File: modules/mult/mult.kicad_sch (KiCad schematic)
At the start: 9 parts, among them J1 Thonkiconn, J2 Thonkiconn, J3 Thonkiconn, J4 Thonkiconn, J5 Thonkiconn, J6 Thonkiconn, J7 Thonkiconn, J8 Thonkiconn

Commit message: Generate KiCad projects from Haskell: pcbgen toolkit, regenerated mult
toolkit/ is a cabal project that turns a design description
(toolkit/src/Designs/<Name>.hs) into a complete KiCad 10 project: schematic
with embedded library symbols, board with embedded library footprints, project
file with design rules, and custom DRC rules. UUIDs are derived from stable
seeds so regeneration is byte-identical. toolkit/check.sh runs ERC, DRC with
zone refill and schematic parity on a copy in build/, and renders both sides.

modules/mult is now generated. With --severity-all it has zero ERC violations,
zero DRC violations, zero unconnected items and zero parity issues. The
Konnect-made board it replaces had nine library-mismatch warnings and needed
GUI steps to finish.

README.md explains the tool choices (KiCad as compile target, kicad-cli,
KiKit for fab export, Konnect read-only). SETUP.md and CLAUDE.md follow the
new workflow.

Co-Authored-By: Claude Fable 5.1 <noreply@anthropic.com>
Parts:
- JP1: now left out of the parts list
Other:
- note added: "MULT - passive 2x4 multiple, 4HP J1-J4 = group A, J5-J8 = group B. Bridge JP1 (back of PCB) to join both groups into one 1x8 multiple. Jack switch (TN) pins intentionally unconnected."
- note removed: "MULT - passive 2x4 multiple, 4HP J1-J4 = group A, J5-J8 = group B. Bridge JP1 to join both groups into one 1x8 multiple. Jack switch (TN) pins intentionally unconnected."
- title: (none) -> MULT - passive 2x4 multiple

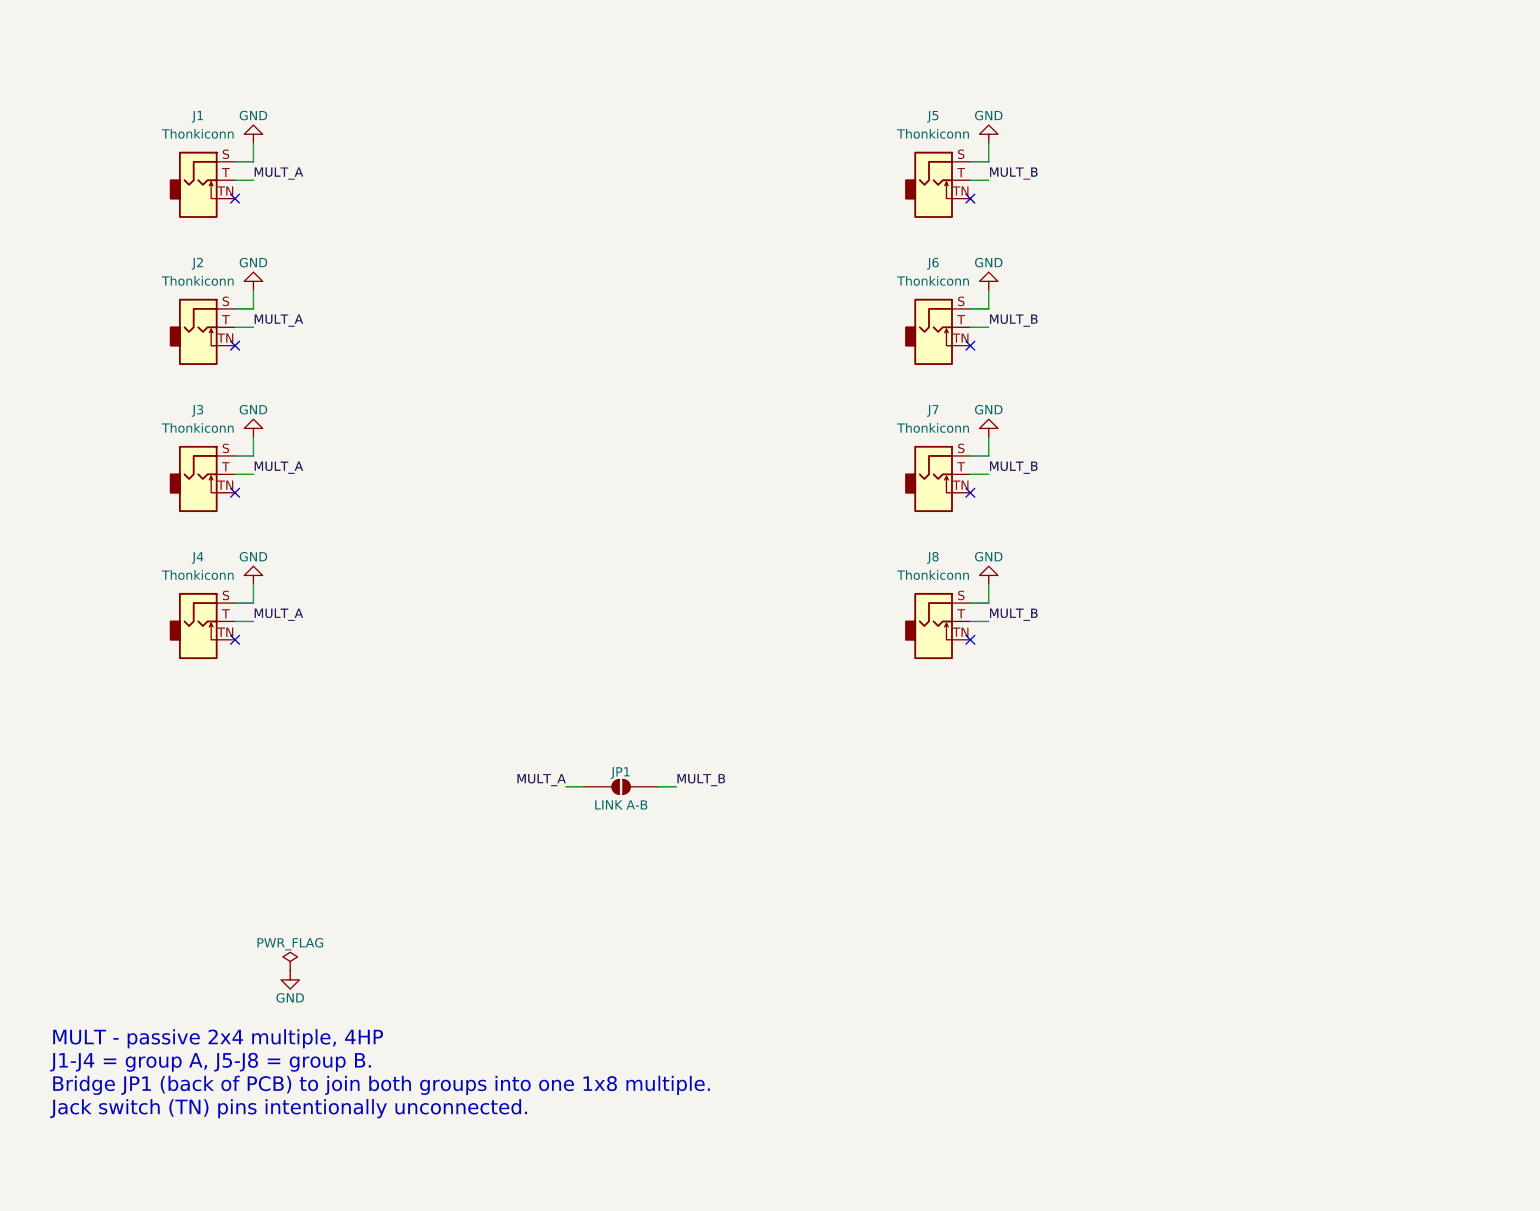
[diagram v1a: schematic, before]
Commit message: Fix Eurorack dimensions: mult becomes 6HP 2x6, add panel project and KiKit export
Doepfer's construction notes and the rail-clearance consensus (PCB <= 108 mm,
centred) showed the 4HP eight-jack column could not fit: the official
Thonkiconn footprint forces a 13.6 mm pitch, and eight of them plus the
barrel and the last body need 110.7 mm. The module is now 6HP with two
columns of six on a 28 x 108 mm board centred behind a 30 x 128.5 mm panel.

- Design.eurorackPanelWidth uses Doepfer's width table; panel height is a
  named constant.
- Designs.MultPanel generates the front panel as its own KiCad project
  (modules/mult/panel) from the same geometry; rail holes at Doepfer
  positions, 6.4 mm jack holes, legend on F.SilkS.
- pcbgen gains 'all' and per-design output directories; parts can hide
  their reference on silkscreen.
- check.sh takes a module sub-directory; fab.sh runs KiKit 1.8.1 (installed
  in KiCad's Python) with --no-drc because its own DRC pass crashes in the
  KiCad 10 bindings. Gerber extents verified: 28.00 x 108.00 and
  30.00 x 128.50 mm.
- Both projects: ERC clean, DRC clean with parity, zero unconnected.

Co-Authored-By: Claude Fable 5.1 <noreply@anthropic.com>
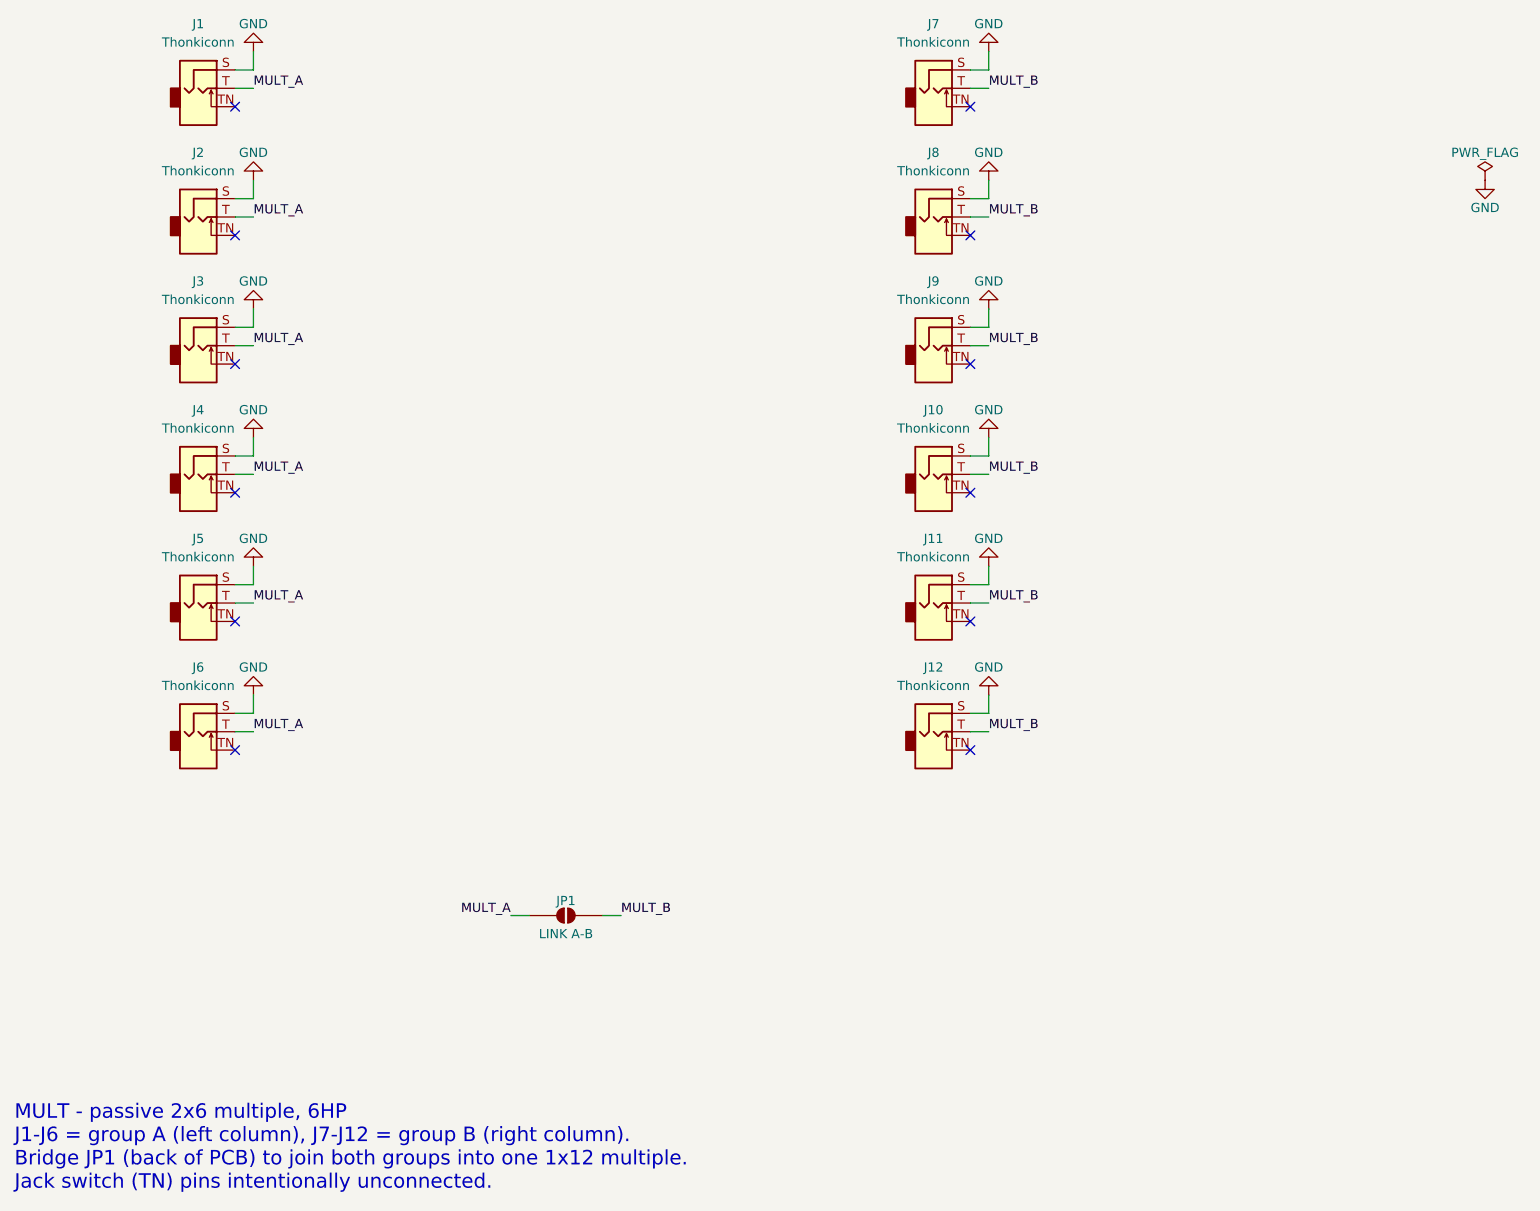
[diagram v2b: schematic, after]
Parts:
- added J10, J11, J12, J9: Thonkiconn, Connector_Audio:Jack_3.5mm_QingPu_WQP-PJ398SM_Vertical_CircularHoles, symbol Connector_Audio:AudioJack2_SwitchT
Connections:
- net GND: now also J10.S, J11.S, J12.S, J9.S
- net MULT_A: now also J5.T, J6.T
- net MULT_B: now also J10.T, J11.T, J12.T, J9.T; no longer J5.T, J6.T
- no-connect marks 8 -> 12
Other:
- note added: "MULT - passive 2x6 multiple, 6HP J1-J6 = group A (left column), J7-J12 = group B (right column). Bridge JP1 (back of PCB) to join both groups into one 1x12 multiple. Jack switch (TN) pins intentionally unconnected."
- note removed: "MULT - passive 2x4 multiple, 4HP J1-J4 = group A, J5-J8 = group B. Bridge JP1 (back of PCB) to join both groups into one 1x8 multiple. Jack switch (TN) pins intentionally unconnected."
- title: MULT - passive 2x4 multiple -> MULT - passive 2x6 multiple
- moved on the sheet: J1, J2, J3, J4, J5, J6, J7, J8, JP1
